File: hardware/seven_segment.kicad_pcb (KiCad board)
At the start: 4 copper layers, 74 x 34 mm, 36 parts, among them J1 Conn_01x16, J2 PJ-102AH, J3 Conn_01x04, J5 Conn_01x06, SW2 SW_Push, U1 ESP32-WROOM-32E, U2 ULN2003A, U3 ULN2003A, U4 TPS562200, U5 74HC595, U6 74HC595, U7 ULN2003A

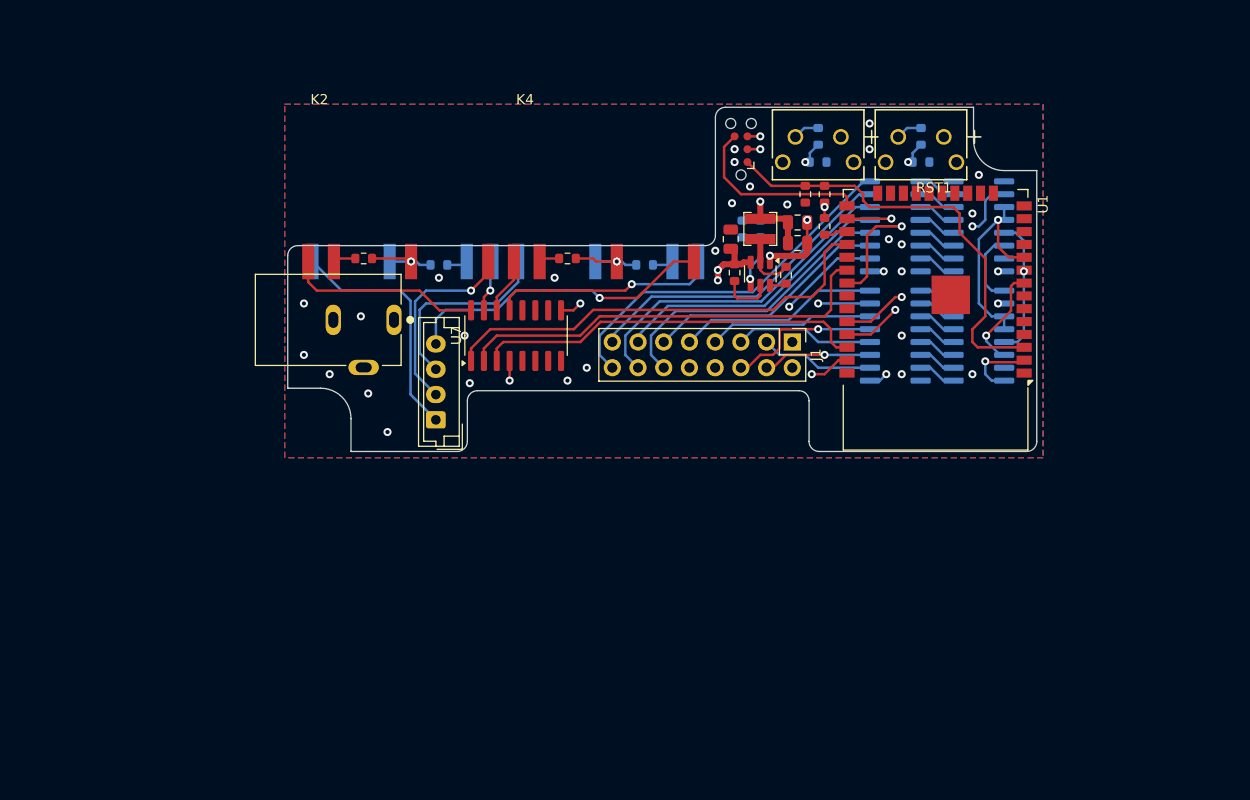
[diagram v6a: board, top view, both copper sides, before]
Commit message: hardware: revision 4
Changelog:
Load switching:
        - Move back to transistors rather than relays since they are
          more reliable, faster and quiter.
Mechanics:
        - Ditch the hammond enclosure for a 3d-printed chassi.
        - Connectors are now located on the back-side of the PCB, the
          idea is to cut out holes in the display backside to pass
          through cables.
UI:
        - Add 2 LEDs
        - Remove a button
Power:
        - Remove 12V connector in favor of USB-C
        - Step up/down the required 12/3.3V from the USB 5V
Other:
        - Clean up repo structure
        - Remove unused libraries
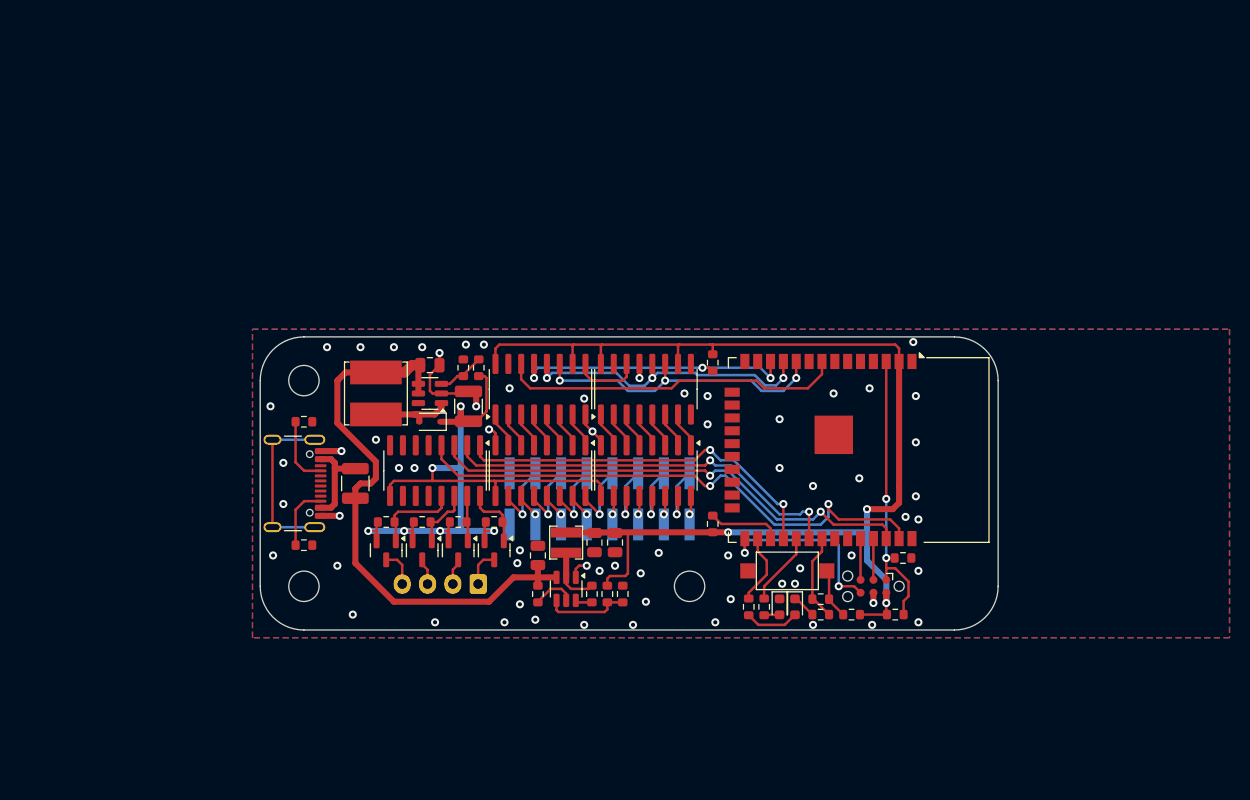
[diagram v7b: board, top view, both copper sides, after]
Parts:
- removed C1: C, Resistor_SMD:R_0603_1608Metric
- removed J5: Conn_01x06, Connector:Tag-Connect_TC2030-IDC-NL_2x03_P1.27mm_Vertical
- removed K1, K2, K3, K4: ~, 00_customfootprints:G6DN-1A-SL
- removed RST1, SW2: SW_Push, pushbutton:TO_6083716_WRE
- added C5: 22uF, Capacitor_SMD:C_0805_2012Metric, F.Cu at (114.0, 125.5)
- added C6: 2.2uF, Capacitor_SMD:C_1210_3225Metric, F.Cu at (117.9, 129.5)
- added D1: 1N5819WS, Diode_SMD:D_SOD-323, F.Cu at (114.0, 131.1)
- added D2: LED, LED_SMD:LED_0603_1608Metric, F.Cu at (150.1, 149.4)
- added D3: LED, LED_SMD:LED_0603_1608Metric, F.Cu at (148.6, 149.4)
- added F1: Polyfuse, Resistor_SMD:R_1210_3225Metric, F.Cu at (106.7, 137.2)
- added H1: MountingHole, MountingHole:MountingHole_3mm, F.Cu at (101.6, 147.3)
- added H2: MountingHole, MountingHole:MountingHole_3mm, F.Cu at (139.7, 147.3)
- added H3: MountingHole, MountingHole:MountingHole_3mm, F.Cu at (101.6, 127.0)
- added J4: ~, Connector_PinHeader_2.54mm:PinHeader_2x08_P2.54mm_Vertical_SMD, B.Cu at (130.8, 138.7)
- added L2: 22uH, Inductor_SMD:L_Bourns_SRN6045TA, F.Cu at (108.7, 128.3)
- added Q1: IRLML5203, Package_TO_SOT_SMD:SOT-23, F.Cu at (120.4, 143.8)
- added Q2: IRLML5203, Package_TO_SOT_SMD:SOT-23, F.Cu at (116.8, 143.8)
- added Q3: IRLML5203, Package_TO_SOT_SMD:SOT-23, F.Cu at (113.3, 143.8)
- added Q4: IRLML5203, Package_TO_SOT_SMD:SOT-23, F.Cu at (109.7, 143.8)
- added R12: 10k, Resistor_SMD:R_0603_1608Metric, F.Cu at (118.9, 125.7)
- added R13: 510, Resistor_SMD:R_0603_1608Metric, F.Cu at (117.3, 125.7)
- added R14: 5.1k, Resistor_SMD:R_0603_1608Metric, F.Cu at (101.6, 143.3)
- added R15: 5.1k, Resistor_SMD:R_0603_1608Metric, F.Cu at (101.6, 131.1)
- added R16: 47, Resistor_SMD:R_0603_1608Metric, F.Cu at (145.5, 149.4)
- added R17: 47, Resistor_SMD:R_0603_1608Metric, F.Cu at (147.1, 149.4)
- added R19: 10k, Resistor_SMD:R_0603_1608Metric, F.Cu at (142.0, 125.2)
- added SW1: SW_Push, Button_Switch_SMD:SW_SPST_CK_RS282G05A3, F.Cu at (149.4, 145.8)
- added U8: MT3608, Package_TO_SOT_SMD:SOT-23-6, F.Cu at (114.0, 128.3)
- C2: value C -> 1nF; moved to F.Cu
- C3: value 10p -> 1nF
- J1: value Conn_01x16 -> ~; footprint Connector_PinHeader_2.54mm:PinHeader_2x08_P2.54mm_Vertical -> Connector:Tag-Connect_TC2030-IDC-NL_2x03_P1.27mm_Vertical
- J2: value PJ-102AH -> USB_C_Receptacle_USB2.0_16P; footprint PJ_102AH:CUI_PJ-102AH -> Connector_USB:USB_C_Receptacle_GCT_USB4105-xx-A_16P_TopMnt_Horizontal
- J3: moved to B.Cu
- R10, R9, U2, U3, U5, U6: moved to F.Cu
- R3, R4, R5, R7: value R -> 10k; moved to F.Cu
- R6, R8: value R -> 10k
- moved R4 47.7 mm to (155.7, 150.1), turned to 180 degrees
- moved R5 45.7 mm to (152.7, 148.6), turned to 0 degrees
- moved C2 44.7 mm to (152.7, 150.1), turned to 180 degrees
- moved U5 43.6 mm to (125.0, 127.8), turned to 90 degrees
- moved R2 42.1 mm to (160.0, 150.1), turned to 0 degrees
- moved R9 39.1 mm to (131.6, 148.1)
- moved R10 38.0 mm to (133.1, 148.1)
- moved U2 37.5 mm to (125.0, 135.9), turned to -90 degrees
- moved R11 37.2 mm to (124.7, 148.1)
- moved C3 37.2 mm to (160.8, 144.5), turned to 0 degrees
- moved C4 36.9 mm to (130.0, 148.1)
- moved U6 36.6 mm to (135.4, 127.8), turned to 90 degrees
- moved C9 36.6 mm to (124.7, 144.3)
- moved U4 36.5 mm to (127.5, 147.6)
- moved L1 36.4 mm to (127.5, 143.0)
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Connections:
- net /sreg_data renamed /mosi
- C2 pad 1: Net-(U1-IO4) -> Net-(U1-IO19)
- C3 pad 1: /EN -> Net-(J1-EN)
- C9 pad 1: +12V -> VBUS
- J1 pad 1: unconnected-(J1-Pin_1-Pad1) -> Net-(J1-EN)
- J1 pad 2: unconnected-(J1-Pin_2-Pad2) -> +3V3
- J1 pad 3: /clr_d -> /TXD0
- J1 pad 4: /set_d -> GND
- J1 pad 5: /clr_e -> /RXD0
- J1 pad 6: /set_c -> /IO0
- R11 pad 1: +12V -> VBUS
- R2 pad 2: /EN -> Net-(J1-EN)
- R3 pad 1: Net-(K1-Pad2) -> +12V
- R3 pad 2: +12V -> Net-(Q1-G)
- R4 pad 1: Net-(U1-IO19) -> +3V3
- R5 pad 1: Net-(U1-IO4) -> Net-(U1-IO19)
- R5 pad 2: Net-(R5-Pad2) -> Net-(R4-Pad2)
- R6 pad 1: Net-(K2-Pad2) -> +12V
- R6 pad 2: +12V -> Net-(Q2-G)
- R7 pad 1: Net-(K3-Pad2) -> +12V
- R7 pad 2: +12V -> Net-(Q3-G)
- R8 pad 1: Net-(K4-Pad2) -> +12V
- R8 pad 2: +12V -> Net-(Q4-G)
- U1 pad 10: /sreg_sclk -> /sclk
- U1 pad 11: unconnected-(U1-IO26-Pad11) -> /rclk
- U1 pad 12: unconnected-(U1-IO27-Pad12) -> /sr_oe
- U1 pad 29: unconnected-(U1-IO5-Pad29) -> Net-(U1-IO5)
- U1 pad 3: /EN -> Net-(J1-EN)
- U1 pad 9: /sreg_oe -> unconnected-(U1-IO33-Pad9)
- U2 pad 10: /clr_d -> Net-(J4-D_clr)
- U2 pad 11: /set_d -> Net-(J4-D_set)
- U2 pad 12: /clr_e -> Net-(J4-E_clr)
- U2 pad 13: /set_c -> Net-(J4-C_set)
- U2 pad 14: /set_e -> Net-(J4-E_set)
- U2 pad 15: /clr_c -> Net-(J4-C_clr)
- U2 pad 16: /clr_f -> Net-(J4-F_clr)
- U3 pad 10: /set_b -> Net-(J4-B_set)
- U3 pad 11: /set_f -> Net-(J4-F_set)
- U3 pad 12: /clr_b -> Net-(J4-B_clr)
- U3 pad 13: /set_g -> Net-(J4-G_set)
- U3 pad 14: /set_a -> Net-(J4-A_set)
- U3 pad 15: /clr_g -> Net-(J4-G_clr)
- U3 pad 16: /clr_a -> Net-(J4-A_clr)
- U4 pad 3: +12V -> VBUS
- U5 pad 11: /sreg_sclk -> /sclk
- U5 pad 12: /sreg_sclk -> /rclk
- U5 pad 13: /sreg_oe -> /sr_oe
- U6 pad 11: /sreg_sclk -> /sclk
- U6 pad 12: /sreg_sclk -> /rclk
- U6 pad 13: /sreg_oe -> /sr_oe
- U7 pad 13: Net-(U7-O4) -> Net-(Q4-G)
- U7 pad 14: Net-(U7-O3) -> Net-(Q3-G)
- U7 pad 15: Net-(U7-O2) -> Net-(Q2-G)
- U7 pad 16: Net-(U7-O1) -> Net-(Q1-G)
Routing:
- net +3V3: track 29.3 -> 120.2 mm, vias 7 -> 3
- net VBUS: track 0.00 -> 60.2 mm
- net +12V: track 28.4 -> 76.1 mm, vias 7 -> 6
- net /EN: track 43.0 -> 0.00 mm
- net /TXD0: track 47.0 -> 4.08 mm, vias 2 -> 0
- net /RXD0: track 43.1 -> 4.08 mm, vias 2 -> 0
- net /clr_a: track 36.7 -> 0.00 mm
- net /set_a: track 33.1 -> 0.00 mm
- net /clr_g: track 31.9 -> 0.00 mm
- net /sr_oe: track 0.00 -> 31.2 mm, vias 0 -> 4
- net /sclk: track 0.00 -> 30.1 mm, vias 0 -> 3
- net /rclk: track 0.00 -> 29.9 mm, vias 0 -> 3
- net /clr_b: track 29.5 -> 0.00 mm
- net Net-(J1-EN): track 0.00 -> 28.8 mm, vias 0 -> 2
- net /set_g: track 28.3 -> 0.00 mm
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- removed copper zone on In2.Cu, net +12V
- removed copper zone on In2.Cu, net +3V3
- removed copper zone on In1.Cu, net GND
- removed copper zone on In2.Cu, net GND
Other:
- board size 74 x 34 mm -> 72.9 x 29 mm
- copper layers 4 -> 2
- board text removed: "Hammond 1551KBK max.height 10.4mm"
